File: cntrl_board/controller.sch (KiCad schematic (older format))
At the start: 0 parts

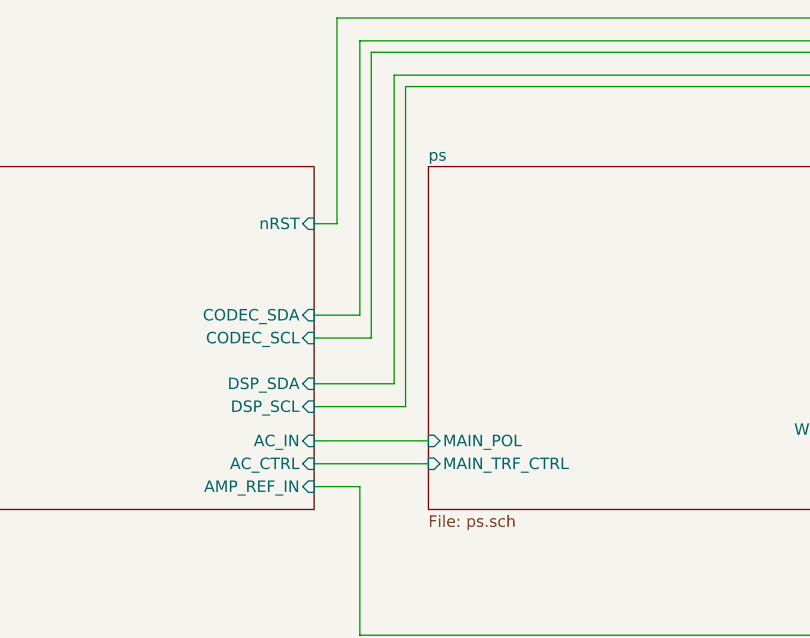
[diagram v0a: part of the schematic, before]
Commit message: update xformer soft startup
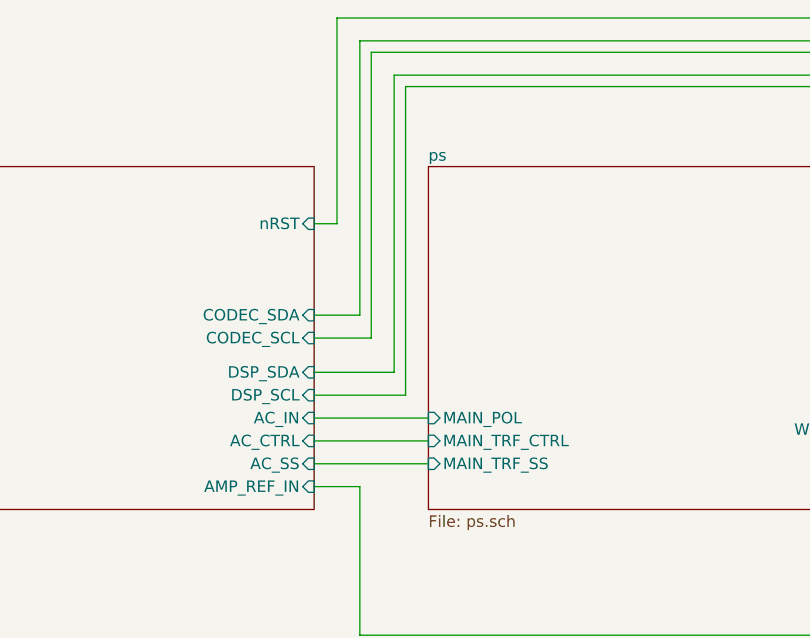
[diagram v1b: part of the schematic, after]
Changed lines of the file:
@@
 F3 "CODEC_SDA" I R 6000 3650 50
 F4 "CODEC_SCL" I R 6000 3750 50
-F5 "DSP_SDA" I R 6000 3950 50
-F6 "DSP_SCL" I R 6000 4050 50
-F7 "AC_IN" I R 6000 4200 50
-F8 "AC_CTRL" I R 6000 4300 50
+F5 "DSP_SDA" I R 6000 3900 50
+F6 "DSP_SCL" I R 6000 4000 50
+F7 "AC_IN" I R 6000 4100 50
+F8 "AC_CTRL" I R 6000 4200 50
 F9 "AMP_REF_IN" I R 6000 4400 50
+F10 "AC_SS" I R 6000 4300 50
 $EndSheet
 $Sheet
@@
 F0 "ps" 50
 F1 "ps.sch" 50
-F2 "MAIN_TRF_CTRL" I L 6500 4300 50
-F3 "MAIN_POL" I L 6500 4200 50
+F2 "MAIN_TRF_CTRL" I L 6500 4200 50
+F3 "MAIN_POL" I L 6500 4100 50
 F4 "WR_BACK" I R 8500 4150 50
 F5 "nRST" I R 8500 4000 50
+F6 "MAIN_TRF_SS" I L 6500 4300 50
 $EndSheet
 $Sheet
@@
 	13750 4250 13500 4250
 Wire Wire Line
-	6000 4200 6500 4200
-Wire Wire Line
-	6500 4300 6000 4300
-Wire Wire Line
-	6000 4050 6400 4050
-Wire Wire Line
-	6400 4050 6400 2650
-Wire Wire Line
 	6400 2650 8850 2650
 Wire Wire Line
 	8800 2600 6350 2600
 Wire Wire Line
-	6350 2600 6350 3950
-Wire Wire Line
-	6350 3950 6000 3950
+	6350 2600 6350 3900
 Wire Wire Line
 	6000 3750 6250 3750
@@
 Wire Wire Line
 	13500 3900 13850 3900
+Wire Wire Line
+	6000 3900 6350 3900
+Wire Wire Line
+	6000 4000 6400 4000
+Wire Wire Line
+	6400 4000 6400 2650
+Wire Wire Line
+	6000 4100 6500 4100
+Wire Wire Line
+	6500 4200 6000 4200
+Wire Wire Line
+	6000 4300 6500 4300
 $EndSCHEMATC
